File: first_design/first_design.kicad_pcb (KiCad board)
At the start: 2 copper layers, 65 x 56.5 mm, 53 parts, among them J1 Conn_02x20_Odd_Even, J2 Accelerometer_small, J3 Accelerometer_standard, J4 Servo_motor

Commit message: traced buck
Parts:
- C9: footprint library_express_pro:RLC_EIA_3216 -> library_express_pro:Capacitor_E61
- J1: footprint library_express_pro:RasPi_header_pro -> library_express_pro:RasPi_Header_0.9
- L1: footprint library_express_pro:RLC_EIA_3216 -> library_express_pro:Inductor_PA4340
- moved None1 43.8 mm to (-5.23, -9.00)
- moved AI1027TWT5V2R1 40.5 mm to (37.5, -6.50)
- moved R_IR1 35.3 mm to (45.0, -44.5), turned to 270 degrees
- moved VoltageMonitor1 31.3 mm to (23.0, -30.0), turned to 270 degrees
- moved R4 25.2 mm to (46.5, -34.5)
- moved 2N7002K1 20.4 mm to (46.5, -40.0)
- moved C3 18.4 mm to (17.5, -25.0), turned to 270 degrees
- moved C2 18.0 mm to (22.0, -25.0), turned to 90 degrees
- moved R5 17.0 mm to (41.5, -14.0), turned to 270 degrees
- moved C1 16.5 mm to (41.5, -20.5), turned to 270 degrees
- moved R1_buck1 16.2 mm to (33.5, -18.5), turned to 270 degrees
- moved JP1 14.9 mm to (29.5, -6.00)
- moved R2_buck1 12.0 mm to (26.5, -18.5), turned to 90 degrees
- moved C6 10.7 mm to (24.5, -37.0), turned to 90 degrees
- moved C5 10.4 mm to (30.0, -20.5), turned to 90 degrees
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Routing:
- net +5V: track 0.00 -> 48.7 mm
- net Net-(2N7002K2-Pad2): track 0.00 -> 38.6 mm, vias 0 -> 2
- net GND: track 10.9 -> 48.3 mm, vias 25 -> 39
- net Net-(R1_buck1-Pad2): track 0.00 -> 19.3 mm
- net (no net): track 0.00 -> 18.8 mm, vias 0 -> 4
- net Net-(2N7002K2-Pad1): track 0.00 -> 9.05 mm
- net Net-(AI1027TWT5V2R1-Pad1): track 0.00 -> 7.48 mm
- net Net-(C6-Pad1): track 0.00 -> 6.65 mm
- net motor_INA: track 1.34 -> 7.43 mm
- net Net-(Rmax1-Pad1): track 22.2 -> 28.3 mm
- net Net-(C4-Pad2): track 0.00 -> 5.93 mm
- net Net-(C5-Pad2): track 0.00 -> 4.78 mm
- net motor_INB: track 2.40 -> 3.40 mm
- added copper zone on B.Cu, net +5V
- added copper zone on F.Cu, net +5V
- added copper zone on F.Cu, net Net-(C6-Pad2)

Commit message: Stuck trying to trace Pi connector pins. Need some tips
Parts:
- moved J3 48.5 mm to (42.0, -45.0), turned to 0 degrees
- moved J2 46.5 mm to (42.5, -47.5), turned to 0 degrees
- moved 2N7002K1 9.01 mm to (46.0, -31.0)
- moved R4 9.01 mm to (46.0, -25.5)
- moved R_IR1 8.06 mm to (46.0, -36.5)
- moved PTS636_G_Leads4 1.12 mm to (54.0, -10.0)
- moved PTS636_G_Leads1 1.00 mm to (54.0, -32.0)
- moved PTS636_G_Leads2 1.00 mm to (54.0, -21.0)
- moved PTS636_G_Leads3 1.00 mm to (54.0, -43.0)
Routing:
- net (no net): track 18.8 -> 0.00 mm, vias 4 -> 0
- net +5V: track 48.7 -> 67.6 mm, vias 0 -> 4
- net SCL: track 0.00 -> 2.96 mm
- net SDA: track 0.00 -> 2.74 mm
- net +3.3V: track 0.00 -> 2.71 mm
- net GND: track 48.3 -> 50.9 mm
- net Net-(Rmax1-Pad1): track 28.3 -> 30.8 mm

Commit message: Before changes
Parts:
- removed C3: 100nF, library_express_pro:RLC_EIA_3216
- removed C8: 10uF, library_express_pro:RLC_EIA_3216
- removed R10, R7, R8, R9: 220, library_express_pro:RLC_EIA_3216
- removed R11, R12, R13, R14: 82, library_express_pro:RLC_EIA_3216
- added U1: Resistor_array, library_express_pro:Resistor_array_YC324, F.Cu at (85.0, -33.0)
- R1: value 220 -> 22.1
- R2: value 220 -> 66.3
- R4, R5: value 10K -> 22.1K
- Rmax1: value 280 -> 22.1K
- moved Button3 3.00 mm to (57.0, -32.0)
- moved Button4'1 3.00 mm to (51.0, -43.0)
- renumbered PTS636_G_Leads4 to Button1, PTS636_G_Leads2 to Button2, PTS636_G_Leads1 to Button3, PTS636_G_Leads3 to Button4'1
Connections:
- net +7.5V renamed VDC
- net 6V-5V renamed servo
- Button4'1 pad 1: Net-(PTS636_G_Leads3-Pad1) -> +3.3V
- J1 pad 14: Net-(J1-Pad14) -> GND
- J1 pad 15: IR_Transmitter -> Net-(J1-Pad15)
- J1 pad 2: Net-(J1-Pad2) -> +5V
- J1 pad 20: Net-(J1-Pad20) -> GND
- J1 pad 25: Net-(J1-Pad25) -> GND
- J1 pad 30: Net-(J1-Pad30) -> GND
- J1 pad 34: Net-(J1-Pad34) -> GND
- J1 pad 39: Net-(J1-Pad39) -> GND
- J1 pad 9: Net-(J1-Pad9) -> GND
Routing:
- net GND: track 50.9 -> 51.9 mm

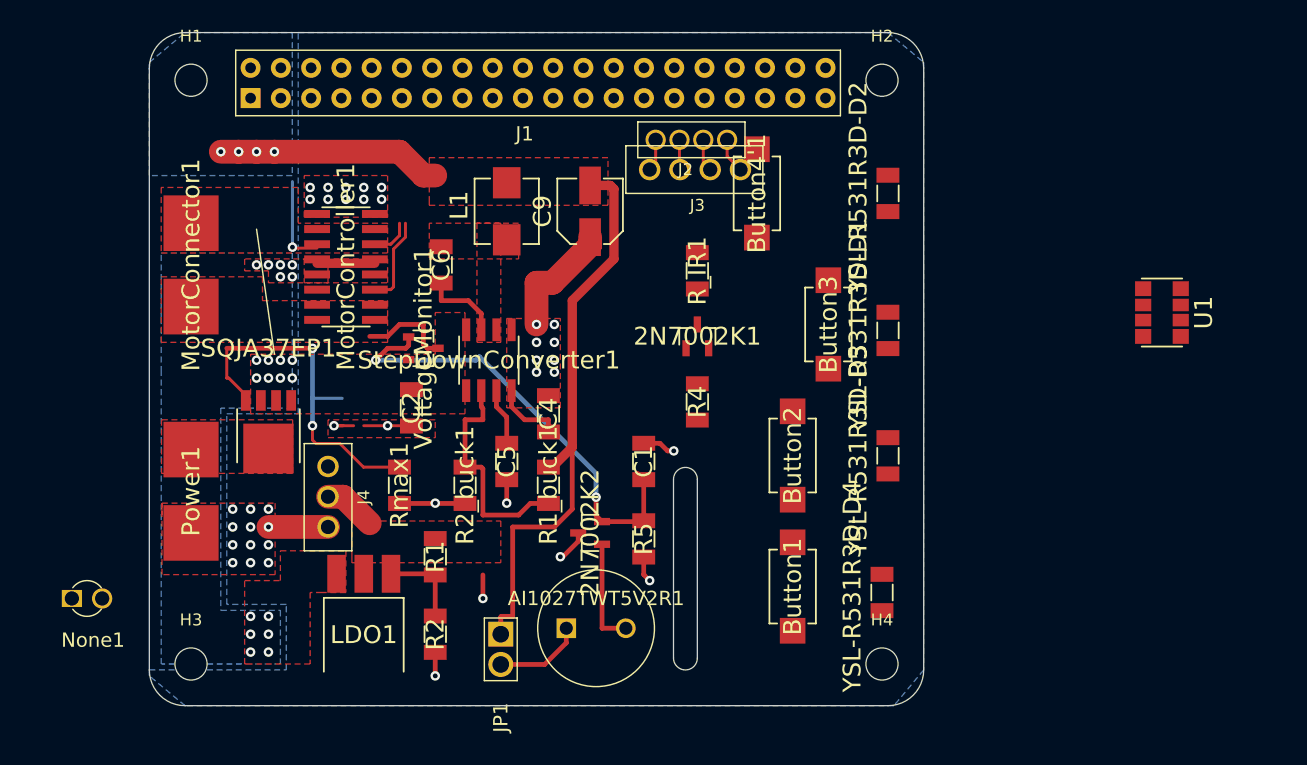
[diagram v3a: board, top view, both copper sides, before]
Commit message: working on tracing, back layer is messed up
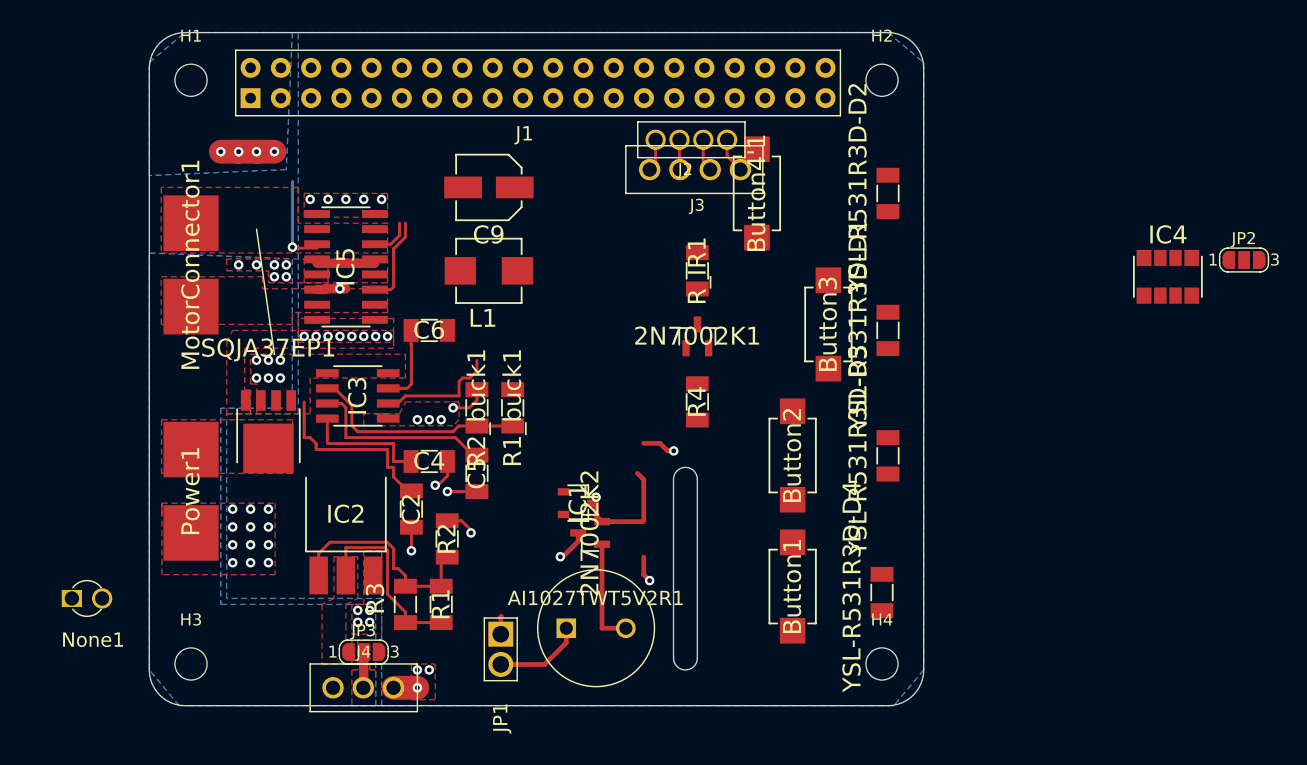
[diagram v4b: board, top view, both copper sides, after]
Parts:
- removed C1: 10uF, library_express_pro:RLC_EIA_3216
- removed R5, Rmax1: 22.1K, library_express_pro:RLC_EIA_3216
- removed U1: Resistor_array, library_express_pro:Resistor_array_YC324
- added IC4: RN, library_express_pro:Resistor_array_YC324, F.Cu at (85.5, -36.0)
- added JP2: SolderJumper_3_Bridged12, Jumper:SolderJumper-3_P1.3mm_Open_RoundedPad1.0x1.5mm_NumberLabels, F.Cu at (91.9, -37.4)
- added JP3: SolderJumper_3_Bridged12, Jumper:SolderJumper-3_P1.3mm_Open_RoundedPad1.0x1.5mm_NumberLabels, F.Cu at (18.0, -4.50)
- added R3: 66.3k, library_express_pro:RLC_EIA_3216, F.Cu at (21.5, -8.50)
- R1: value 22.1 -> 22.1k
- R2: value 66.3 -> 66.3k
- YSL-R531R3D-D1: value LED -> LED2
- YSL-R531R3D-D2: value LED -> LED1
- YSL-R531R3D-D3: value LED -> LED3
- YSL-R531R3D-D4: value LED -> LED4
- moved IC1 18.4 mm to (36.0, -17.0)
- moved J4 16.3 mm to (18.0, -1.50), turned to 180 degrees
- moved IC3 11.4 mm to (17.5, -26.0), turned to 270 degrees
- moved C4 10.8 mm to (23.5, -20.5), turned to 180 degrees
- moved C9 8.73 mm to (28.5, -43.5), turned to 180 degrees
- moved C2 8.50 mm to (22.0, -16.5)
- moved IC2 8.14 mm to (16.5, -15.0), turned to 0 degrees
- moved R2 8.06 mm to (25.0, -14.0), turned to 90 degrees
- moved R1_buck1 7.16 mm to (30.5, -25.0)
- moved R2_buck1 6.58 mm to (27.5, -25.0), turned to 270 degrees
- moved C6 5.59 mm to (23.5, -31.5), turned to 0 degrees
- moved L1 5.22 mm to (28.5, -36.5), turned to 180 degrees
- moved R1 4.03 mm to (24.5, -8.50), turned to 90 degrees
- moved C5 2.69 mm to (27.5, -19.5)
- renumbered VoltageMonitor1 to IC1, LDO1 to IC2, StepDownConverter1 to IC3, MotorController1 to IC5
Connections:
- net LED1 renamed GPIO12
- net LED2 renamed GPIO16
- net LED3 renamed GPIO20
- net LED4 renamed GPIO21
- net VDC renamed VCC
- net button1 renamed GPIO26
- net button2 renamed GPIO13
- net button3 renamed GPIO6
- net button4 renamed GPIO5
- net motor_INA renamed GPIO18
- net motor_INB renamed GPIO24
- net motor_PWM renamed GPIO25
- net servo_PWM renamed GPIO23
- AI1027TWT5V2R1 pad 2: Net-(2N7002K2-Pad1) -> Net-(AI1027TWT5V2R1-Pad2)
- IC2 pad 2: servo -> Vservo
- J1 pad 7: Net-(J1-Pad7) -> GND
- J1 pad 9: GND -> Net-(J1-Pad9)
- J4 pad 2: servo -> Net-(J4-Pad2)
- L1 pad 1: Net-(C6-Pad2) -> +5V
- L1 pad 2: +5V -> Net-(C6-Pad2)
- R1 pad 1: servo -> Vservo
- SQJA37EP1 pad 3: Net-(Rmax1-Pad1) -> GND
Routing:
- net +5V: track 67.6 -> 6.02 mm
- net Net-(Rmax1-Pad1): track 30.8 -> 0.00 mm, vias 2 -> 0
- net Net-(2N7002K2-Pad2): track 38.6 -> 9.98 mm, vias 2 -> 1
- net GND: track 51.9 -> 28.6 mm, vias 39 -> 40
- net Vbat: track 4.85 -> 20.3 mm, vias 20 -> 16
- net Vservo: track 0.00 -> 15.1 mm
- net Net-(C5-Pad2): track 4.78 -> 15.8 mm
- net Net-(IC2-Pad1): track 7.20 -> 18.2 mm
- net Net-(C6-Pad2): track 0.00 -> 10.2 mm
- net Net-(C4-Pad2): track 5.93 -> 10.7 mm
- net servo: track 4.42 -> 0.00 mm
- net Net-(J4-Pad2): track 0.00 -> 3.02 mm
- net Net-(IC3-Pad2): track 19.3 -> 18.2 mm
- added copper zone on F.Cu, net Net-(J4-Pad2)
- added copper zone on F.Cu, net Vservo
- removed copper zone on F.Cu, net +5V
- removed copper zone on F.Cu, net Net-(C6-Pad2)
- removed copper zone on F.Cu, net servo

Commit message: Killing it
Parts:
- moved JP2 70.6 mm to (30.0, -3.50)
- moved J2 34.5 mm to (8.00, -47.5), turned to 180 degrees
- moved J3 31.6 mm to (10.5, -47.5)
- moved JP1 11.0 mm to (34.0, -16.0)
- moved 2N7002K2 8.32 mm to (30.0, -10.0), turned to 0 degrees
- moved IC1 6.96 mm to (29.5, -14.5), turned to 180 degrees
- moved L1 4.92 mm to (30.5, -32.0), turned to 270 degrees
- moved C9 4.03 mm to (28.0, -39.5), turned to 0 degrees
- moved R1 2.00 mm to (26.5, -8.50)
- moved R3 2.00 mm to (23.5, -8.50)
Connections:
- IC5 pad 11: GPIO25 -> GPIO24
- IC5 pad 3: GPIO18 -> GPIO23
- IC5 pad 6: GPIO24 -> GPIO18
- J4 pad 3: GPIO23 -> GPIO25
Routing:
- net GPIO25: track 7.60 -> 77.8 mm, vias 1 -> 2
- net +5V: track 6.02 -> 68.0 mm, vias 4 -> 7
- net GPIO24: track 3.40 -> 30.1 mm, vias 0 -> 2
- net GPIO23: track 0.00 -> 25.9 mm, vias 0 -> 2
- net GND: track 28.6 -> 51.6 mm
- net SCL: track 2.96 -> 25.8 mm
- net +3.3V: track 2.71 -> 23.1 mm, vias 0 -> 1
- net SDA: track 2.74 -> 16.4 mm
- net Net-(AI1027TWT5V2R1-Pad2): track 0.00 -> 12.7 mm
- net GPIO18: track 7.43 -> 17.3 mm, vias 0 -> 2
- net Vbat: track 20.3 -> 27.8 mm, vias 16 -> 14
- net Vservo: track 15.1 -> 19.6 mm
- net Net-(2N7002K2-Pad1): track 9.05 -> 5.64 mm
- net Net-(IC2-Pad1): track 18.2 -> 21.5 mm
- net Net-(C6-Pad2): track 10.2 -> 7.19 mm
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- added copper zone on F.Cu, net +5V
- added copper zone on F.Cu, net Net-(C6-Pad2)

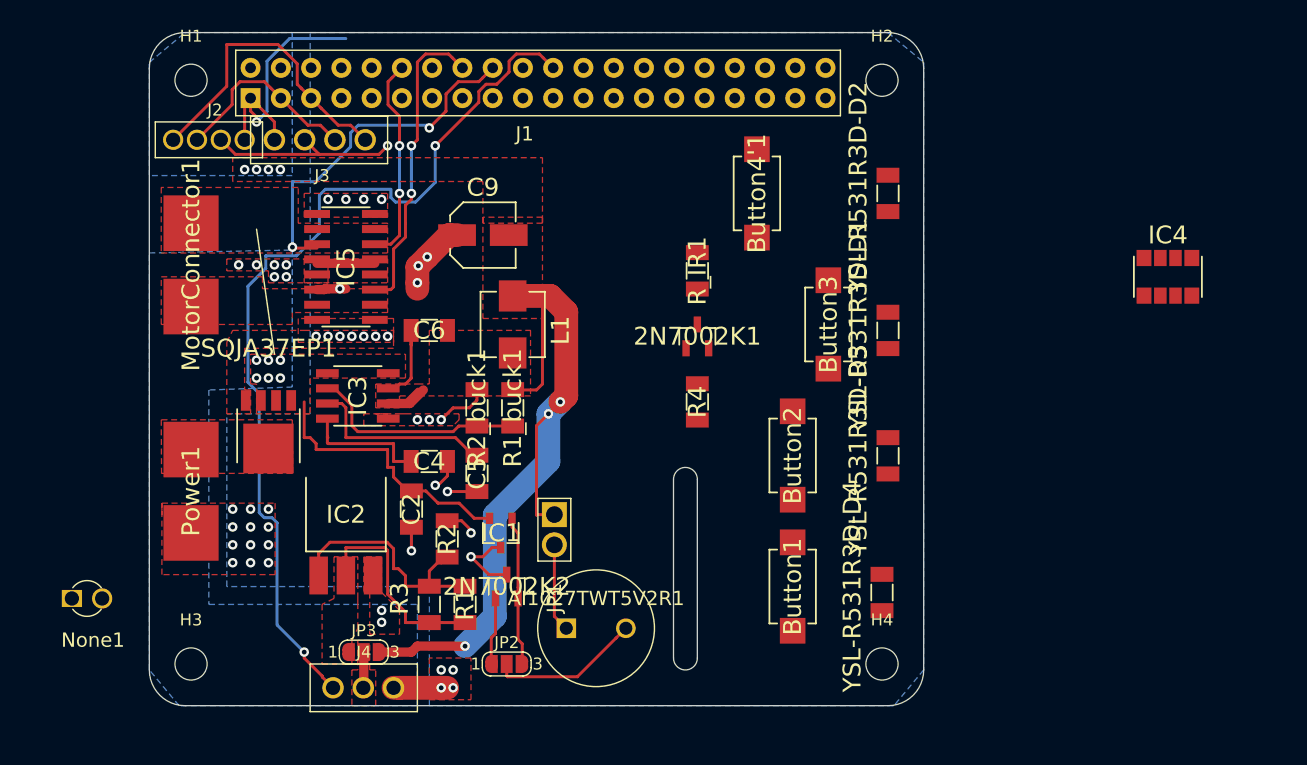
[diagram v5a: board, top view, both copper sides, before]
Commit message: Everything is wired, fixed schematic, haven't found PMOS and IR yet. Check PCB design
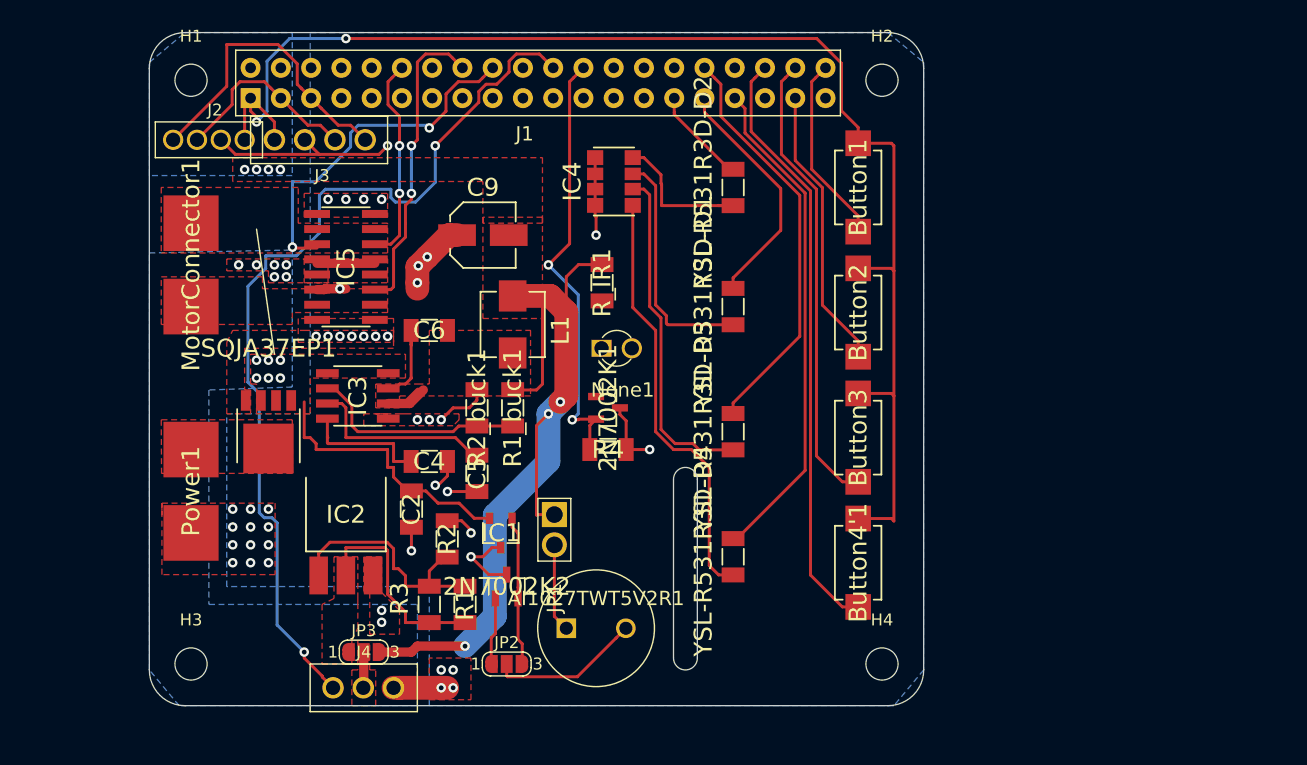
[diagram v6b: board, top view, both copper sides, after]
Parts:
- moved None1 49.2 mm to (39.2, -30.0)
- moved IC4 47.2 mm to (39.0, -44.0), turned to 90 degrees
- moved Button1 33.9 mm to (59.5, -43.5), turned to 270 degrees
- moved Button4'1 32.1 mm to (59.5, -12.0), turned to 270 degrees
- moved Button2 13.2 mm to (59.5, -33.0), turned to 270 degrees
- moved YSL-R531R3D-D3 13.2 mm to (49.0, -23.0)
- moved YSL-R531R3D-D1 13.2 mm to (49.0, -33.5)
- moved YSL-R531R3D-D2 13.0 mm to (49.0, -43.5)
- moved YSL-R531R3D-D4 12.9 mm to (49.0, -12.5)
- moved Button3 9.82 mm to (59.5, -22.5), turned to 270 degrees
- moved 2N7002K1 9.60 mm to (38.5, -25.0), turned to 270 degrees
- moved R4 8.50 mm to (38.5, -21.5), turned to 0 degrees
- moved R_IR1 8.06 mm to (38.0, -35.5), turned to 90 degrees
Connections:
- 2N7002K1 pad 2: IR_Transmitter -> GPIO8
- Button1 pad 2: GPIO26 -> GPIO21
- Button2 pad 2: GPIO13 -> GPIO26
- Button3 pad 2: GPIO6 -> GPIO20
- Button4'1 pad 2: GPIO5 -> GPIO16
- J1 pad 24: Net-(J1-Pad24) -> GPIO8
- R4 pad 1: IR_Transmitter -> GPIO8
- YSL-R531R3D-D1 pad 1: Net-(IC4-Pad2) -> Net-(IC4-Pad3)
- YSL-R531R3D-D1 pad 2: GPIO16 -> GPIO6
- YSL-R531R3D-D2 pad 1: Net-(IC4-Pad1) -> Net-(IC4-Pad4)
- YSL-R531R3D-D2 pad 2: GPIO12 -> GPIO5
- YSL-R531R3D-D3 pad 1: Net-(IC4-Pad3) -> Net-(IC4-Pad2)
- YSL-R531R3D-D3 pad 2: GPIO20 -> GPIO12
- YSL-R531R3D-D4 pad 1: Net-(IC4-Pad4) -> Net-(IC4-Pad1)
- YSL-R531R3D-D4 pad 2: GPIO21 -> GPIO13
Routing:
- net +3.3V: track 23.1 -> 116.7 mm, vias 1 -> 2
- net GPIO16: track 0.00 -> 50.2 mm
- net GPIO13: track 0.00 -> 42.1 mm
- net GPIO20: track 0.00 -> 38.7 mm
- net GPIO8: track 0.00 -> 36.8 mm, vias 0 -> 2
- net Net-(IC4-Pad1): track 0.00 -> 36.1 mm
- net GPIO12: track 0.00 -> 34.6 mm
- net Net-(IC4-Pad2): track 0.00 -> 28.5 mm
- net GPIO26: track 0.00 -> 24.6 mm
- net GPIO6: track 0.00 -> 20.3 mm
- net Net-(IC4-Pad3): track 0.00 -> 19.9 mm
- net GPIO21: track 0.00 -> 15.8 mm
- net Net-(IC4-Pad4): track 0.00 -> 12.8 mm
- net GND: track 51.6 -> 64.0 mm, vias 40 -> 42
- net GPIO5: track 0.00 -> 8.21 mm
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
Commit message: final touches
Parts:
- removed J2: Accelerometer_small, library_express_pro:accelerometer_small
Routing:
- net GPIO25: track 77.8 -> 132.7 mm, vias 2 -> 1
- net SCL: track 25.8 -> 5.99 mm
- net SDA: track 16.4 -> 5.99 mm
- net GND: track 64.0 -> 55.2 mm
- net +3.3V: track 116.7 -> 110.9 mm, vias 2 -> 1

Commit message: final final touches
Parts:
- removed 2N7002K2: NMOS_DGS, library_express_pro:SOT23
- added JP4: SolderJumper_3_Bridged12, Jumper:SolderJumper-3_P1.3mm_Open_RoundedPad1.0x1.5mm_NumberLabels, F.Cu at (33.5, -19.5)
- added Q1: Q_PMOS_DGS, library_express_pro:SOT23, F.Cu at (30.0, -10.0)
- added R_IR2: 220, library_express_pro:RLC_EIA_3216, F.Cu at (30.5, -19.5)
- moved JP2 11.5 mm to (33.5, -14.5), turned to 90 degrees
- moved JP1 3.58 mm to (37.0, -18.0), turned to 0 degrees
- moved None1 0.27 mm to (39.5, -30.0)
- renumbered Button2 to Btn2, Button3 to Btn3, Button4'1 to Btn4
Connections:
- J4 pad 3: GPIO25 -> GPIO12
- JP1 pad 1: +5V -> Net-(JP1-Pad1)
- JP1 pad 2: Net-(AI1027TWT5V2R1-Pad1) -> Net-(AI1027TWT5V2R1-Pad2)
- JP2 pad 2: Net-(AI1027TWT5V2R1-Pad2) -> Net-(AI1027TWT5V2R1-Pad1)
- YSL-R531R3D-D3 pad 2: GPIO12 -> GPIO25
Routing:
- net GPIO12: track 34.6 -> 120.0 mm, vias 0 -> 1
- net GPIO25: track 132.7 -> 48.8 mm, vias 1 -> 0
- net GND: track 55.2 -> 78.6 mm, vias 42 -> 38
- net Net-(JP1-Pad1): track 0.00 -> 4.88 mm
- net Net-(IC1-Pad1): track 12.6 -> 15.4 mm
- net Net-(AI1027TWT5V2R1-Pad1): track 7.41 -> 9.21 mm
- net +5V: track 74.3 -> 75.9 mm
- net Net-(C6-Pad1): track 7.56 -> 6.06 mm
- net Net-(JP2-Pad1): track 5.64 -> 4.41 mm
- net Net-(AI1027TWT5V2R1-Pad2): track 12.7 -> 11.7 mm
